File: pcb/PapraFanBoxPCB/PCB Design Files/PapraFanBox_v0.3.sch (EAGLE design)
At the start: 2 parts

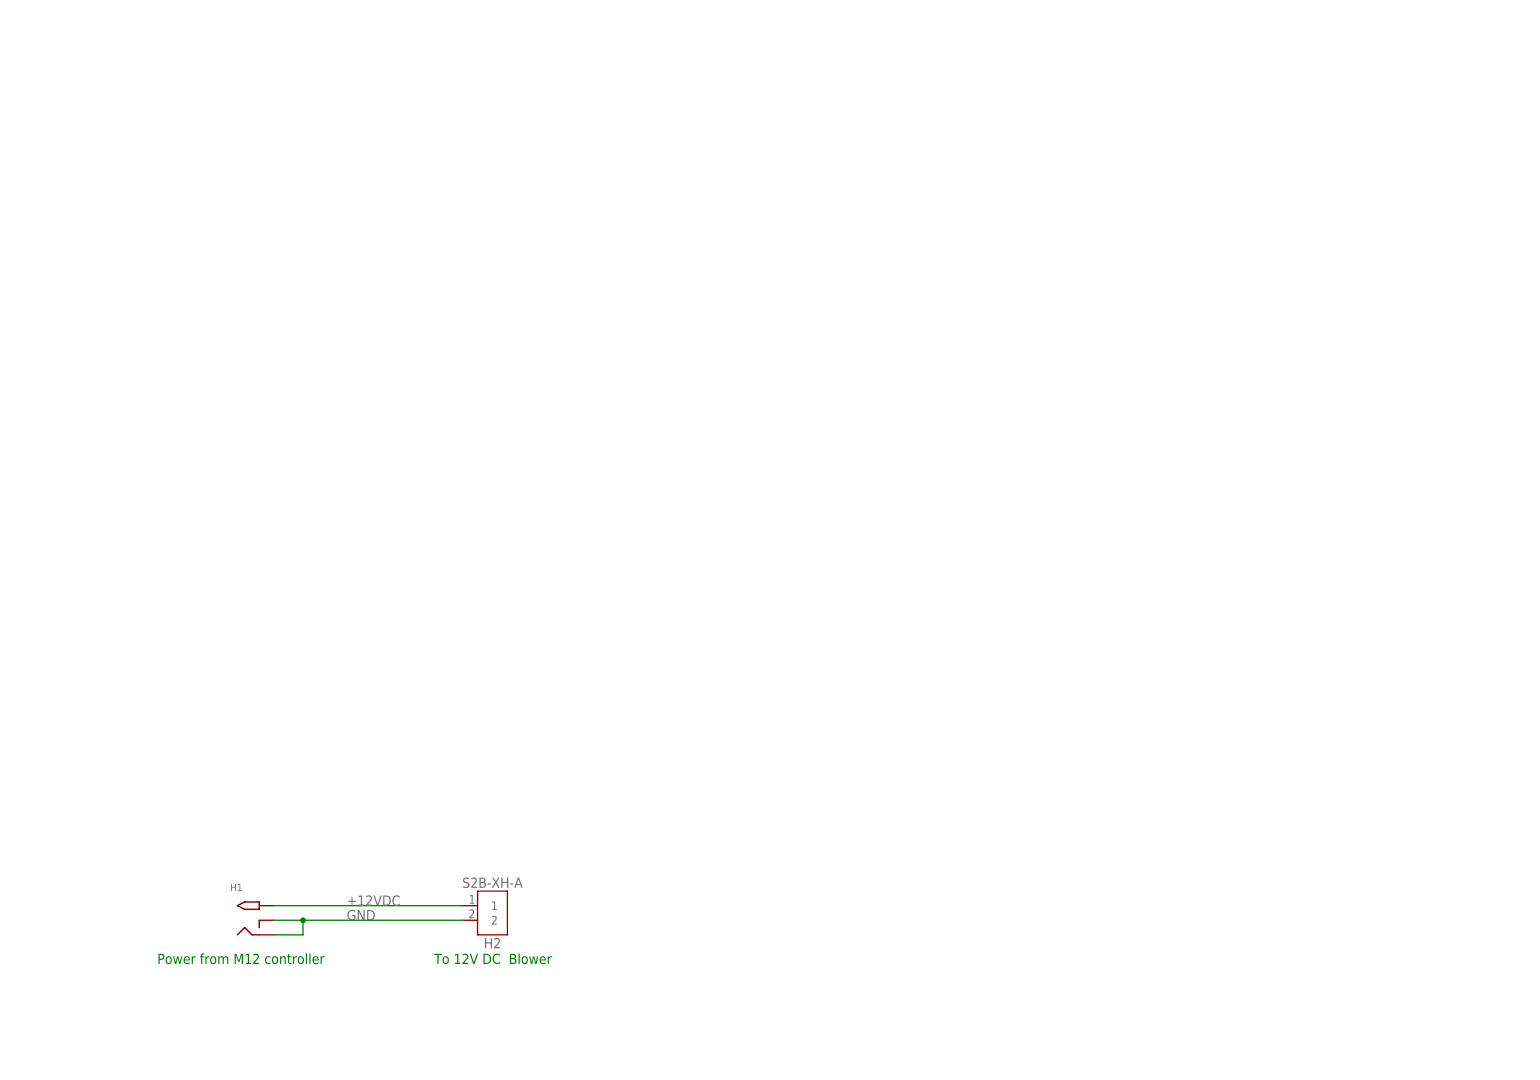
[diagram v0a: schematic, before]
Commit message: Updated fan box PCB to v0.3 (IP68 DC Jack)
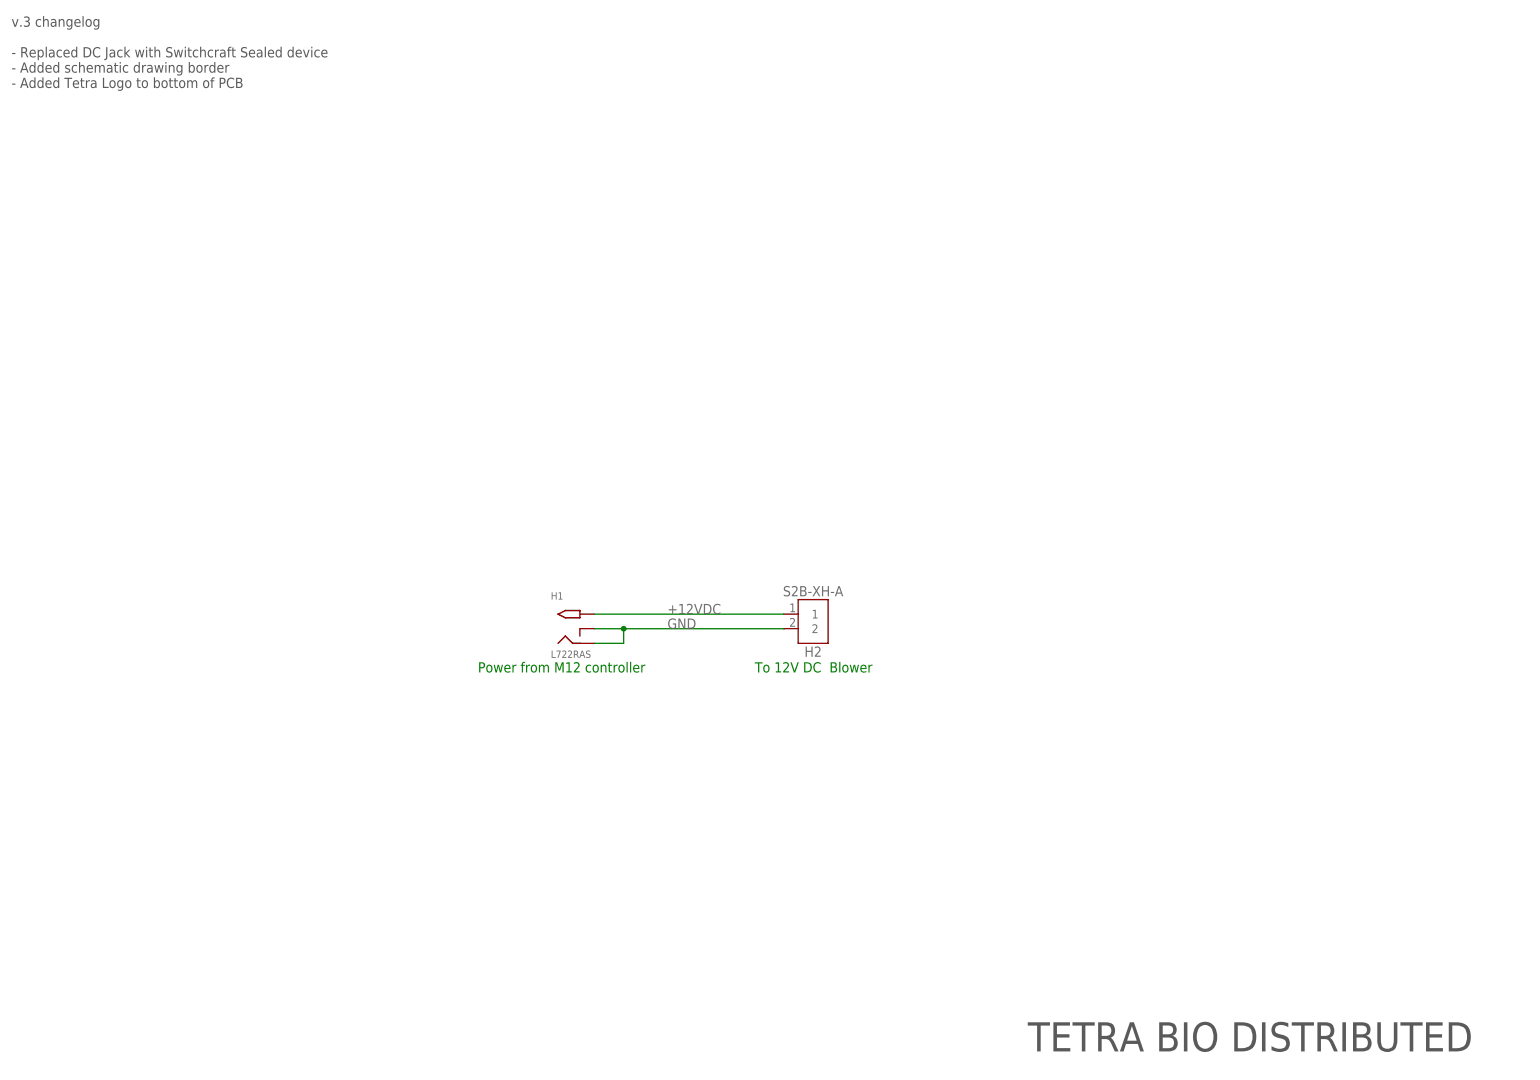
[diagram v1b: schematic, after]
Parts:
- H1: value PJ-066A -> L722RAS; device PC-LIB:PJ-066A -> PC-LIB:SWITCHCRAFT-L722RASSWITCHCRAFTSEALED
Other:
- note added: "TETRA BIO DISTRIBUTED"
- note added: "v.3 changelog - Replaced DC Jack with Switchcraft Sealed device - Added schematic drawing border - Added Tetra Logo to bottom of PCB"
- moved on the sheet: H1, H2
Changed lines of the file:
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@@
 </variantdefs>
 <classes>
-<class number="0" name="default" width="0" drill="0">
+<class number="0" name="default" width="0.254" drill="0">
+<clearance class="0" value="0.2032"/>
+</class>
+<class number="1" name="RAIL" width="0.508" drill="0">
+<clearance class="1" value="0.254"/>
 </class>
 </classes>
 <parts>
 <part name="H2" library="Connector" library_urn="urn:adsk.eagle:library:16378166" deviceset="S2B-XH-A" device="" package3d_urn="urn:adsk.eagle:package:24957651/1"/>
-<part name="H1" library="PC-LIB" deviceset="PJ-066A" device=""/>
+<part name="H1" library="PC-LIB" deviceset="SWITCHCRAFT-L722RAS" device="SWITCHCRAFTSEALED" value="L722RAS"/>
+<part name="FRAME1" library="frames" library_urn="urn:adsk.eagle:library:229" deviceset="FRAME_A_L" device="" value="NONE"/>
 </parts>
 <sheets>
 <sheet>
 <plain>
-<text x="33.02" y="43.18" size="1.778" layer="91">Power from M12 controller</text>
-<text x="81.28" y="43.18" size="1.778" layer="91">To 12V DC  Blower</text>
+<text x="88.9" y="93.98" size="1.778" layer="91">Power from M12 controller</text>
+<text x="137.16" y="93.98" size="1.778" layer="91">To 12V DC  Blower</text>
+<text x="7.62" y="208.28" size="1.778" layer="97" font="vector" align="top-left">v.3 changelog
+- Replaced DC Jack with Switchcraft Sealed device
+- Added schematic drawing border
+- Added Tetra Logo to bottom of PCB
+</text>
+<text x="223.52" y="30.48" size="5.08" layer="97" align="center">TETRA BIO DISTRIBUTED</text>
 </plain>
 <instances>
-<instance part="H2" gate="G$1" x="91.44" y="50.8" smashed="yes">
-<attribute name="NAME" x="91.44" y="46.8" size="1.778" layer="95" align="center"/>
-<attribute name="VALUE" x="91.44" y="57.34" size="1.778" layer="95" align="center"/>
+<instance part="H2" gate="G$1" x="147.32" y="101.6" smashed="yes">
+<attribute name="NAME" x="147.32" y="97.6" size="1.778" layer="95" align="center"/>
+<attribute name="VALUE" x="147.32" y="108.14" size="1.778" layer="95" align="center"/>
 </instance>
-<instance part="H1" gate="G$1" x="50.8" y="50.8" smashed="yes">
-<attribute name="NAME" x="45.72" y="55.88" size="1.27" layer="95"/>
+<instance part="H1" gate="G$1" x="106.68" y="101.6" smashed="yes">
+<attribute name="NAME" x="101.6" y="106.68" size="1.27" layer="95"/>
+<attribute name="VALUE" x="101.6" y="96.52" size="1.27" layer="96"/>
+</instance>
+<instance part="FRAME1" gate="G$1" x="0" y="0" smashed="yes"/>
+<instance part="FRAME1" gate="G$2" x="172.72" y="0" smashed="yes">
+<attribute name="LAST_DATE_TIME" x="185.42" y="1.27" size="2.54" layer="94"/>
+<attribute name="SHEET" x="259.08" y="1.27" size="2.54" layer="94"/>
+<attribute name="DRAWING_NAME" x="190.5" y="19.05" size="2.54" layer="94"/>
 </instance>
 </instances>
@@
 <net name="+12VDC" class="0">
 <segment>
+<pinref part="H2" gate="G$1" pin="1"/>
+<wire x1="109.22" y1="104.14" x2="142.17" y2="104.14" width="0.1524" layer="91"/>
+<label x="121.92" y="104.14" size="1.778" layer="95"/>
 <pinref part="H1" gate="G$1" pin="TIP"/>
-<pinref part="H2" gate="G$1" pin="1"/>
-<wire x1="53.34" y1="53.34" x2="86.29" y2="53.34" width="0.1524" layer="91"/>
-<label x="66.04" y="53.34" size="1.778" layer="95"/>
 </segment>
 </net>
 <net name="GND" class="0">
 <segment>
+<pinref part="H2" gate="G$1" pin="2"/>
+<wire x1="109.22" y1="101.6" x2="114.3" y2="101.6" width="0.1524" layer="91"/>
+<wire x1="114.3" y1="101.6" x2="142.17" y2="101.6" width="0.1524" layer="91"/>
+<wire x1="109.22" y1="99.06" x2="114.3" y2="99.06" width="0.1524" layer="91"/>
+<wire x1="114.3" y1="99.06" x2="114.3" y2="101.6" width="0.1524" layer="91"/>
+<junction x="114.3" y="101.6"/>
+<label x="121.92" y="101.6" size="1.778" layer="95"/>
+<pinref part="H1" gate="G$1" pin="RING"/>
 <pinref part="H1" gate="G$1" pin="RING_SW"/>
-<pinref part="H2" gate="G$1" pin="2"/>
-<wire x1="53.34" y1="50.8" x2="58.42" y2="50.8" width="0.1524" layer="91"/>
-<pinref part="H1" gate="G$1" pin="RING"/>
-<wire x1="58.42" y1="50.8" x2="86.29" y2="50.8" width="0.1524" layer="91"/>
-<wire x1="53.34" y1="48.26" x2="58.42" y2="48.26" width="0.1524" layer="91"/>
-<wire x1="58.42" y1="48.26" x2="58.42" y2="50.8" width="0.1524" layer="91"/>
-<junction x="58.42" y="50.8"/>
-<label x="66.04" y="50.8" size="1.778" layer="95"/>
 </segment>
 </net>
@@
 </drawing>
 <compatibility>
+<note version="6.3" minversion="6.2.2" severity="warning">
+Since Version 6.2.2 text objects can contain more than one line,
+which will not be processed correctly with this version.
+</note>
 <note version="8.2" severity="warning">
 Since Version 8.2, EAGLE supports online libraries. The ids
